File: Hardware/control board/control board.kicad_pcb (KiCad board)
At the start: 2 copper layers, 32 parts, among them J1 Screw_Terminal_01x02, J10 Screw_Terminal_01x02, J11 Screw_Terminal_01x02, J9 Screw_Terminal_01x02, Q1 NMOS, Q2 NMOS, Q3 NMOS, SW1 SW_Push

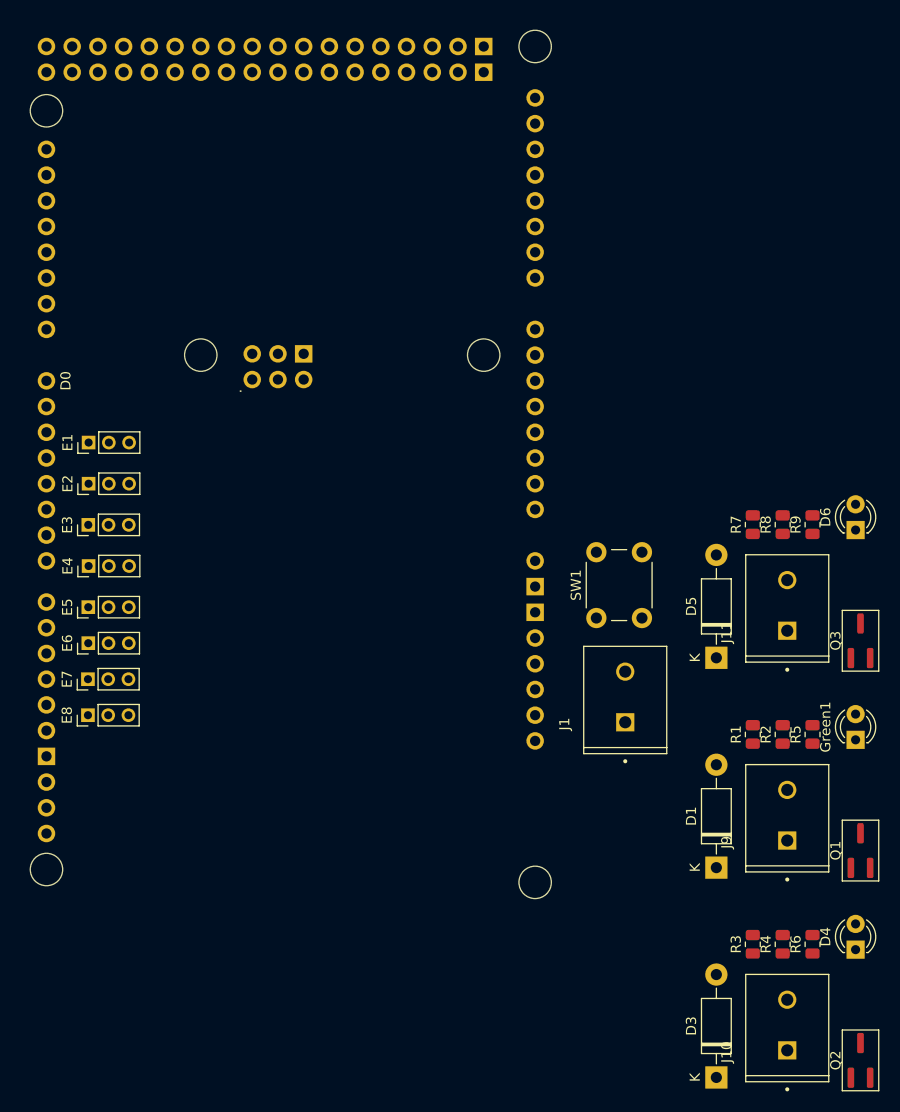
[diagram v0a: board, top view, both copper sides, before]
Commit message: laid out components prior to order
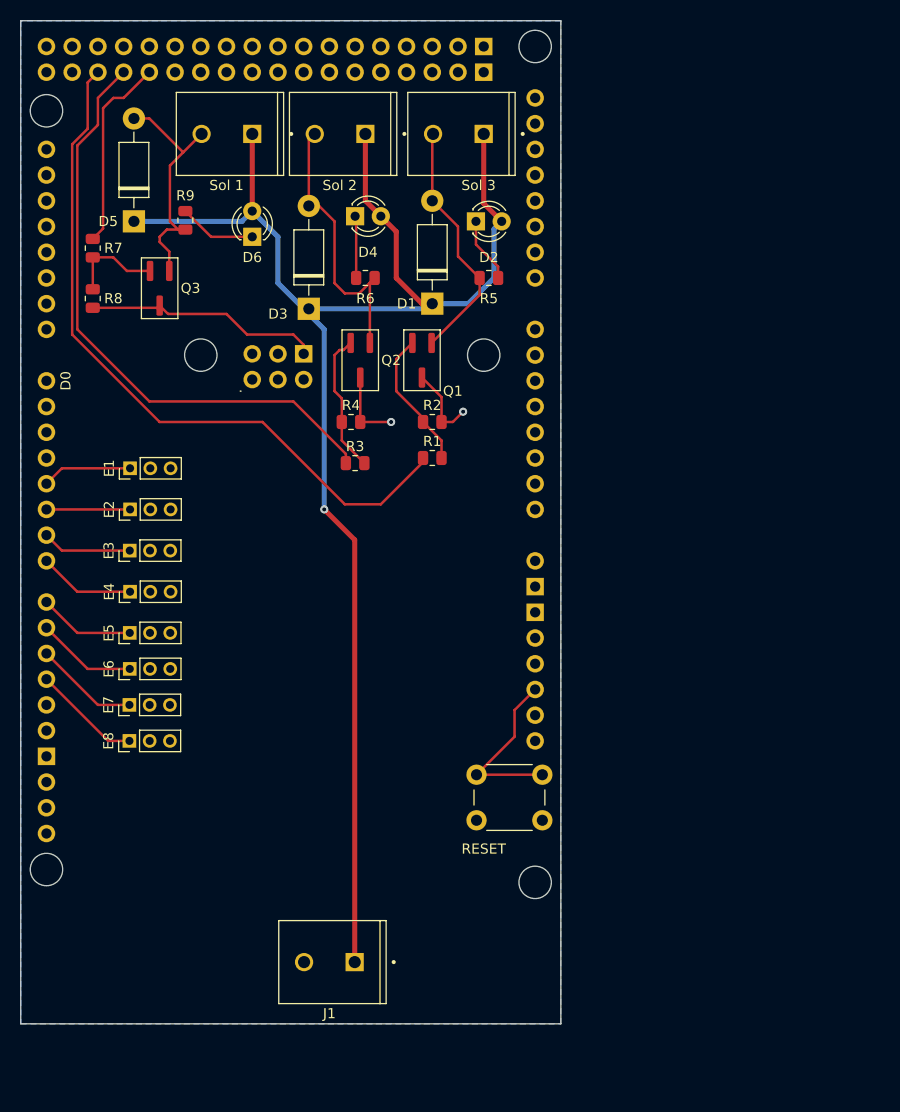
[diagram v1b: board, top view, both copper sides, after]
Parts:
- Sol 1: renamed from J11
- Sol 2: renamed from J10
- Sol 3: renamed from J9
- moved Sol 2 98.5 mm to (63.5, 54.4), turned to 180 degrees
- moved D4 87.7 mm to (65.0, 62.5), turned to 0 degrees
- moved D3 85.9 mm to (60.5, 71.6)
- moved Q2 85.0 mm to (65.5, 76.7), turned to -90 degrees
- moved R6 79.2 mm to (66.0, 68.6), turned to 0 degrees
- moved Q3 77.5 mm to (45.7, 69.6), turned to -90 degrees
- moved Sol 3 74.7 mm to (75.2, 54.4), turned to 180 degrees
- moved Sol 1 72.3 mm to (52.4, 54.4), turned to 180 degrees
- moved D5 71.9 mm to (43.2, 63.0)
- moved R8 71.7 mm to (39.1, 70.6), turned to -90 degrees
- moved R7 70.7 mm to (39.1, 65.6), turned to -90 degrees
- moved R9 68.8 mm to (48.3, 62.9), turned to -90 degrees
- moved R4 66.9 mm to (64.6, 82.8), turned to 0 degrees
- moved D6 66.2 mm to (54.9, 64.5)
- moved Q1 65.0 mm to (71.6, 76.7), turned to -90 degrees
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- renumbered Green1 to D2, SW1 to RESET
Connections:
- A1 pad D23: /solenoid 1/Sol port -> unconnected-(A1-PadD23)
- A1 pad D24: unconnected-(A1-PadD24) -> /solenoid 1/Sol port
- A1 pad D25: /solenoid 2/Sol port -> unconnected-(A1-PadD25)
- A1 pad D26: unconnected-(A1-PadD26) -> /solenoid 2/Sol port
- A1 pad D27: /solenoid 3/Sol port -> unconnected-(A1-PadD27)
- A1 pad D28: unconnected-(A1-PadD28) -> /solenoid 3/Sol port
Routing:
- net +14.8V: track 0.00 -> 153.5 mm, vias 0 -> 1
- net /solenoid 1/Sol port: track 0.00 -> 70.7 mm
- net /solenoid 2/Sol port: track 0.00 -> 59.8 mm
- net GND: track 0.00 -> 38.6 mm, vias 0 -> 2
- net Net-(D3-A): track 0.00 -> 28.2 mm
- net Net-(D5-A): track 0.00 -> 24.6 mm
- net Net-(D1-A): track 0.00 -> 24.6 mm
- net /solenoid 3/Sol port: track 0.00 -> 19.4 mm
- net Net-(A1-RESET): track 0.00 -> 17.3 mm
- net Net-(Q2-G): track 0.00 -> 14.0 mm
- net Net-(Q1-G): track 0.00 -> 13.9 mm
- net /PWMD11: track 0.00 -> 10.7 mm
- net /PWMD10: track 0.00 -> 10.3 mm
- net /PWMD9: track 0.00 -> 9.91 mm
- net /PWMD7: track 0.00 -> 9.52 mm
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- added copper zone on B.Cu, net GND
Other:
- board outline added: 53.3 x 99.1 mm

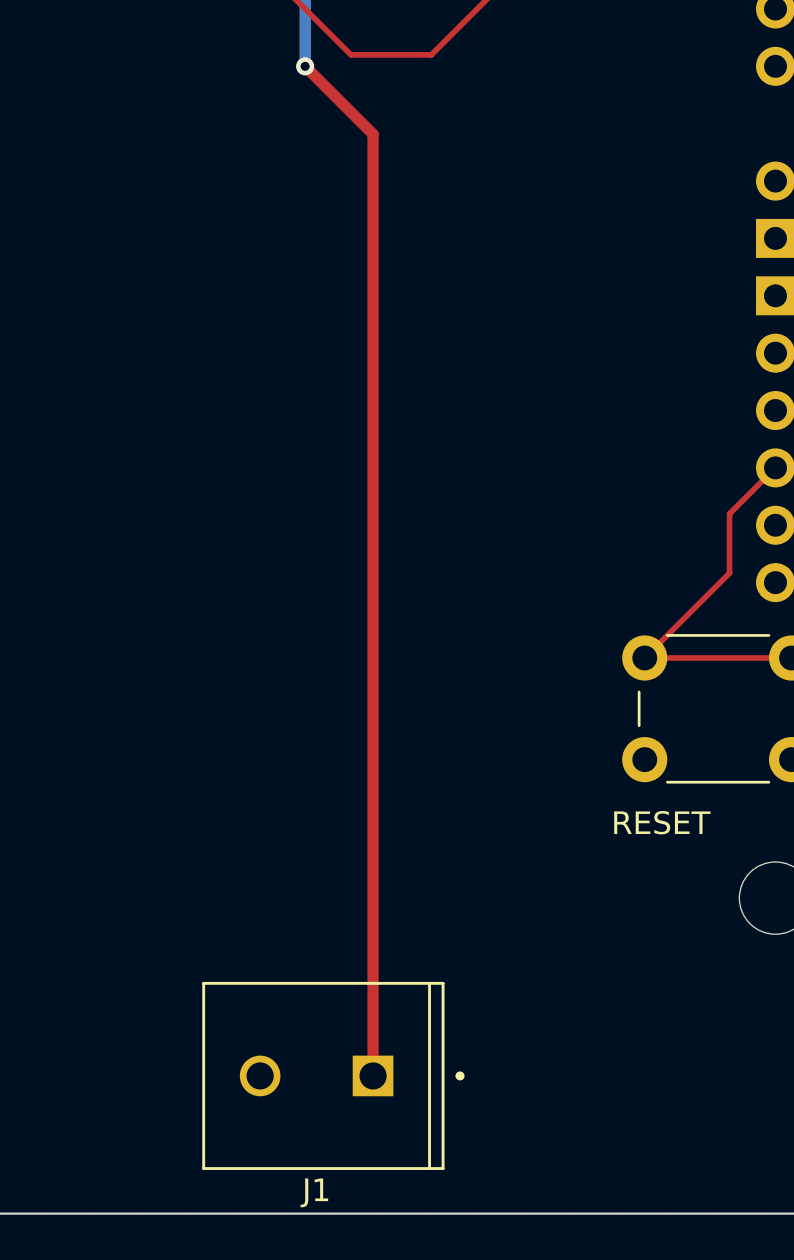
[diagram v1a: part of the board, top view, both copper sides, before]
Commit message: added tags on scrw terminals + logo
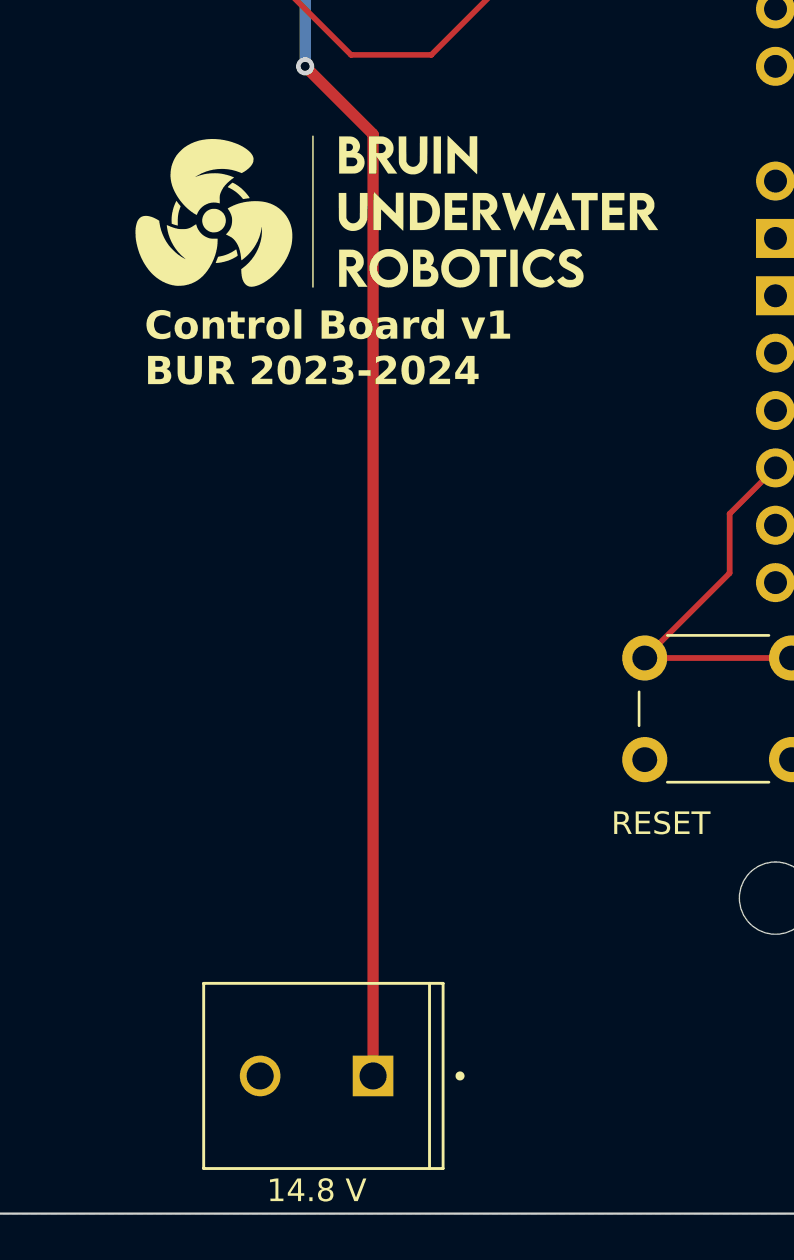
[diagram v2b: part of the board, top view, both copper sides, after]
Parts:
- added G***: LOGO, LOGO, F.Cu at (66.0, 98.0)
- 14.8 V: renamed from J1
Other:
- board text added: "Control Board v1 BUR 2023-2024"

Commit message: control board clean up
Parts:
- removed 14.8 V: Screw_Terminal_01x02, Library:TE_282836-2
- removed RESET: SW_Push, Button_Switch_THT:SW_PUSH_6mm
- removed Sol 1: Screw_Terminal_01x02, Library:TE_282836-2
- removed Sol 2: Screw_Terminal_01x02, Library:TE_282836-2
- removed Sol 3: Screw_Terminal_01x02, Library:TE_282836-2
- added J1: Screw_Terminal_01x02, Library:TE_282836-2, F.Cu at (62.5, 136.1)
- added J10: Screw_Terminal_01x02, Library:TE_282836-2, F.Cu at (63.8, 54.4)
- added J11: Screw_Terminal_01x02, Library:TE_282836-2, F.Cu at (52.3, 54.4)
- added J9: Screw_Terminal_01x02, Library:TE_282836-2, F.Cu at (75.2, 54.4)
- added SW1: SW_Push, Button_Switch_THT:SW_PUSH_6mm, F.Cu at (71.9, 124.4)
- moved E1 4.00 mm to (46.8, 87.4), turned to -90 degrees
- moved E2 4.00 mm to (46.8, 91.4), turned to -90 degrees
- moved E4 4.00 mm to (46.8, 99.6), turned to -90 degrees
- moved E5 4.00 mm to (46.8, 103.6), turned to -90 degrees
- moved E6 4.00 mm to (46.8, 107.2), turned to -90 degrees
- moved E7 4.00 mm to (46.7, 110.7), turned to -90 degrees
- moved E8 4.00 mm to (46.7, 114.3), turned to -90 degrees
- moved E3 3.94 mm to (46.7, 95.5), turned to -90 degrees
- moved D6 1.80 mm to (53.6, 63.2), turned to 0 degrees
- moved D4 0.76 mm to (65.0, 63.2)
- moved R8 0.76 mm to (39.1, 71.4)
- moved R7 0.66 mm to (39.1, 66.3)
- moved D1 0.57 mm to (72.4, 71.6)
- moved R1 0.51 mm to (72.6, 86.9)
- moved R4 0.40 mm to (65.0, 82.8)
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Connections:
- net /solenoid 1/Sol port renamed /sol 1
- net /solenoid 2/Sol port renamed /sol 2
- net /solenoid 3/Sol port renamed /sol 3
- E1 pad 1: /PWMD4 -> GND
- E1 pad 3: GND -> /PWMD4
- E2 pad 1: /PWMD5 -> GND
- E2 pad 3: GND -> /PWMD5
- E3 pad 1: /PWMD6 -> unconnected-(E3-Pin_1-Pad1)
- E3 pad 3: GND -> /PWMD6
- E4 pad 1: /PWMD7 -> GND
- E4 pad 3: GND -> /PWMD7
- E5 pad 1: /PWMD8 -> GND
- E5 pad 3: GND -> /PWMD8
- E6 pad 1: /PWMD9 -> GND
- E6 pad 3: GND -> /PWMD9
- E7 pad 1: /PWMD10 -> GND
- E7 pad 3: GND -> /PWMD10
- E8 pad 1: /PWMD11 -> GND
- E8 pad 3: GND -> /PWMD11
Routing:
- net GND: track 38.6 -> 20.7 mm, vias 2 -> 3
- net Net-(D6-K): track 7.66 -> 4.56 mm
- net /sol 1: track 70.7 -> 68.2 mm
- net Net-(D5-A): track 24.6 -> 22.2 mm
- net +14.8V: track 153.5 -> 155.0 mm
- net Net-(Q2-G): track 14.0 -> 12.8 mm
- net Net-(D3-A): track 28.2 -> 27.1 mm
- net Net-(Q1-G): track 13.9 -> 13.1 mm
- net /sol 2: track 59.8 -> 59.3 mm
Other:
- board text added: "14.8V"
- board text added: "sol 1"
- board text added: "sol 2"
- board text added: "sol 3"

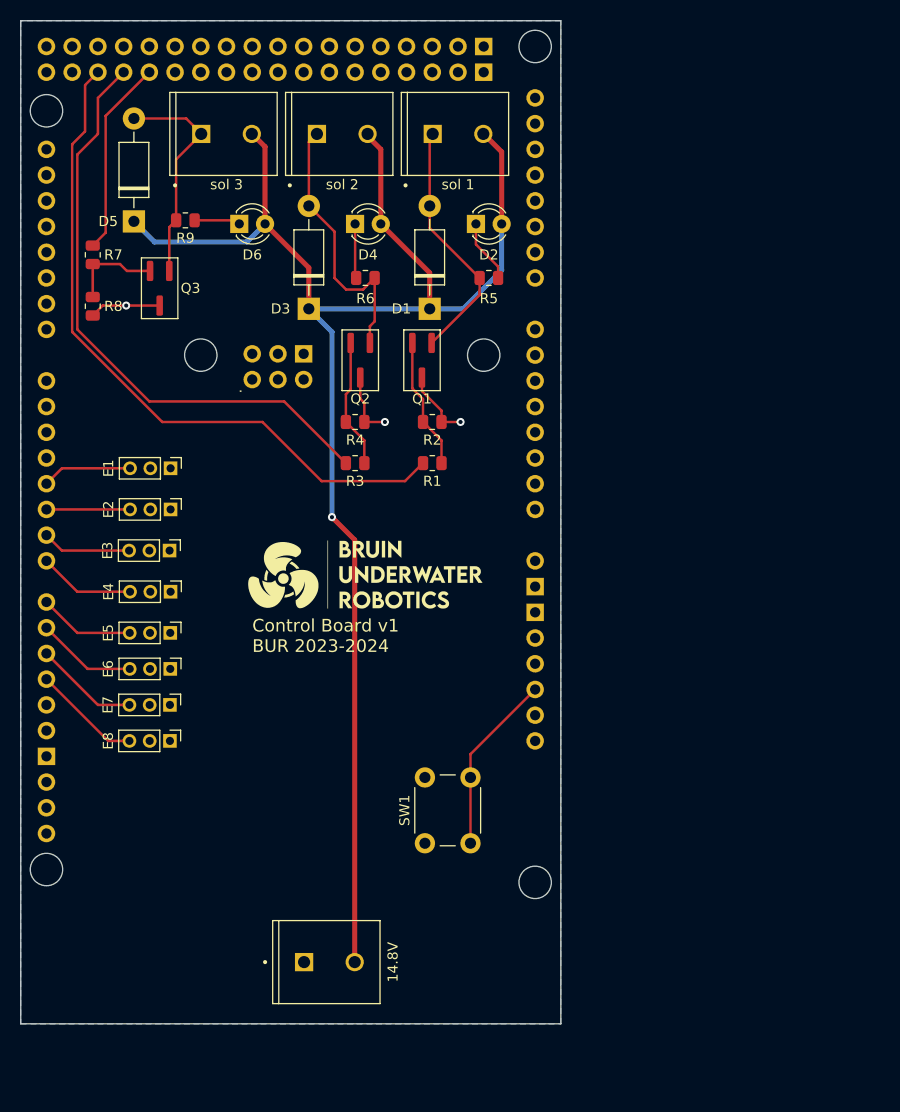
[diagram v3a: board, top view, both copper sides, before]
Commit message: fixed nmos footprint
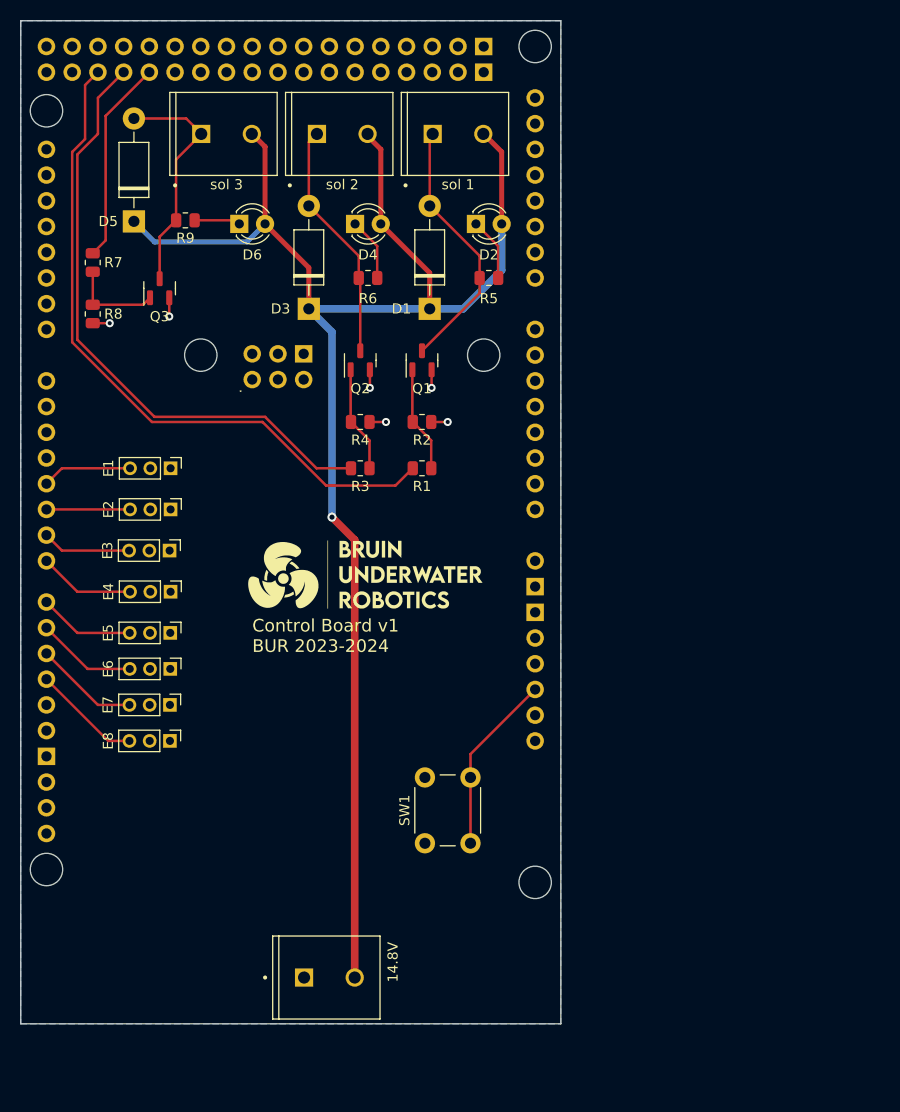
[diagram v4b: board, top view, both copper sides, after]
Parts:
- Q1, Q2, Q3: footprint PCM_Package_TO_SOT_SMD_AKL:TSOT-23_BigPads -> Package_TO_SOT_SMD:SOT-23
- moved J1 1.52 mm to (62.5, 137.7)
- moved R1 1.14 mm to (71.6, 87.4)
- moved R2 1.02 mm to (71.6, 82.8)
- moved R7 0.76 mm to (39.1, 67.1)
- moved R8 0.76 mm to (39.1, 72.1)
- moved R3 0.72 mm to (65.5, 87.4)
- moved R4 0.51 mm to (65.5, 82.8)
- moved R6 0.25 mm to (66.3, 68.6), turned to 180 degrees
- turned Q1 to 90 degrees
- turned Q2 to 90 degrees
- turned Q3 to 90 degrees
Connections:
- E3 pad 1: unconnected-(E3-Pin_1-Pad1) -> GND
- Q1 pad 1: Net-(D1-A) -> Net-(Q1-G)
- Q1 pad 2: Net-(Q1-G) -> GND
- Q1 pad 3: GND -> Net-(D1-A)
- Q2 pad 1: Net-(D3-A) -> Net-(Q2-G)
- Q2 pad 2: Net-(Q2-G) -> GND
- Q2 pad 3: GND -> Net-(D3-A)
- Q3 pad 1: Net-(D5-A) -> Net-(Q3-G)
- Q3 pad 2: Net-(Q3-G) -> GND
- Q3 pad 3: GND -> Net-(D5-A)
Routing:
- net GND: track 20.7 -> 10.4 mm, vias 3 -> 6
- net Net-(D3-A): track 27.1 -> 23.9 mm
- net Net-(Q1-G): track 13.1 -> 9.99 mm
- net Net-(Q2-G): track 12.8 -> 10.0 mm
- net +14.8V: track 155.0 -> 156.5 mm
- net /sol 2: track 59.3 -> 60.6 mm
- net Net-(D5-A): track 22.2 -> 23.3 mm
- net Net-(D1-A): track 24.8 -> 26.0 mm
- net /sol 3: track 19.4 -> 20.2 mm
